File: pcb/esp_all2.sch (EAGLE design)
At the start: 22 parts

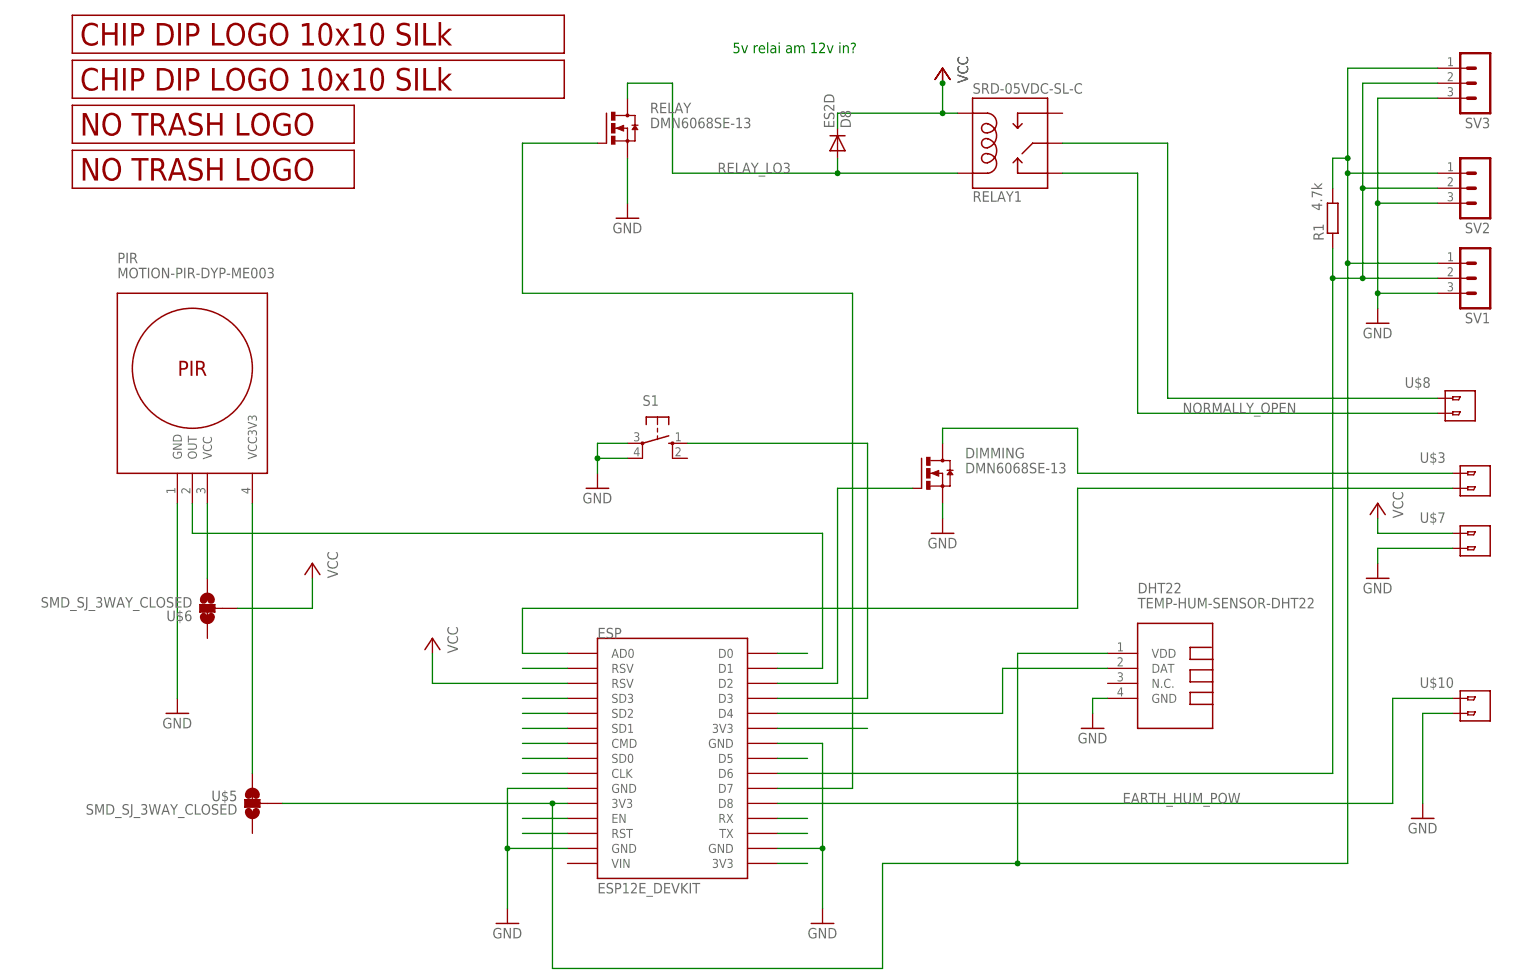
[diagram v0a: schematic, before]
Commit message: Improved ESP readability
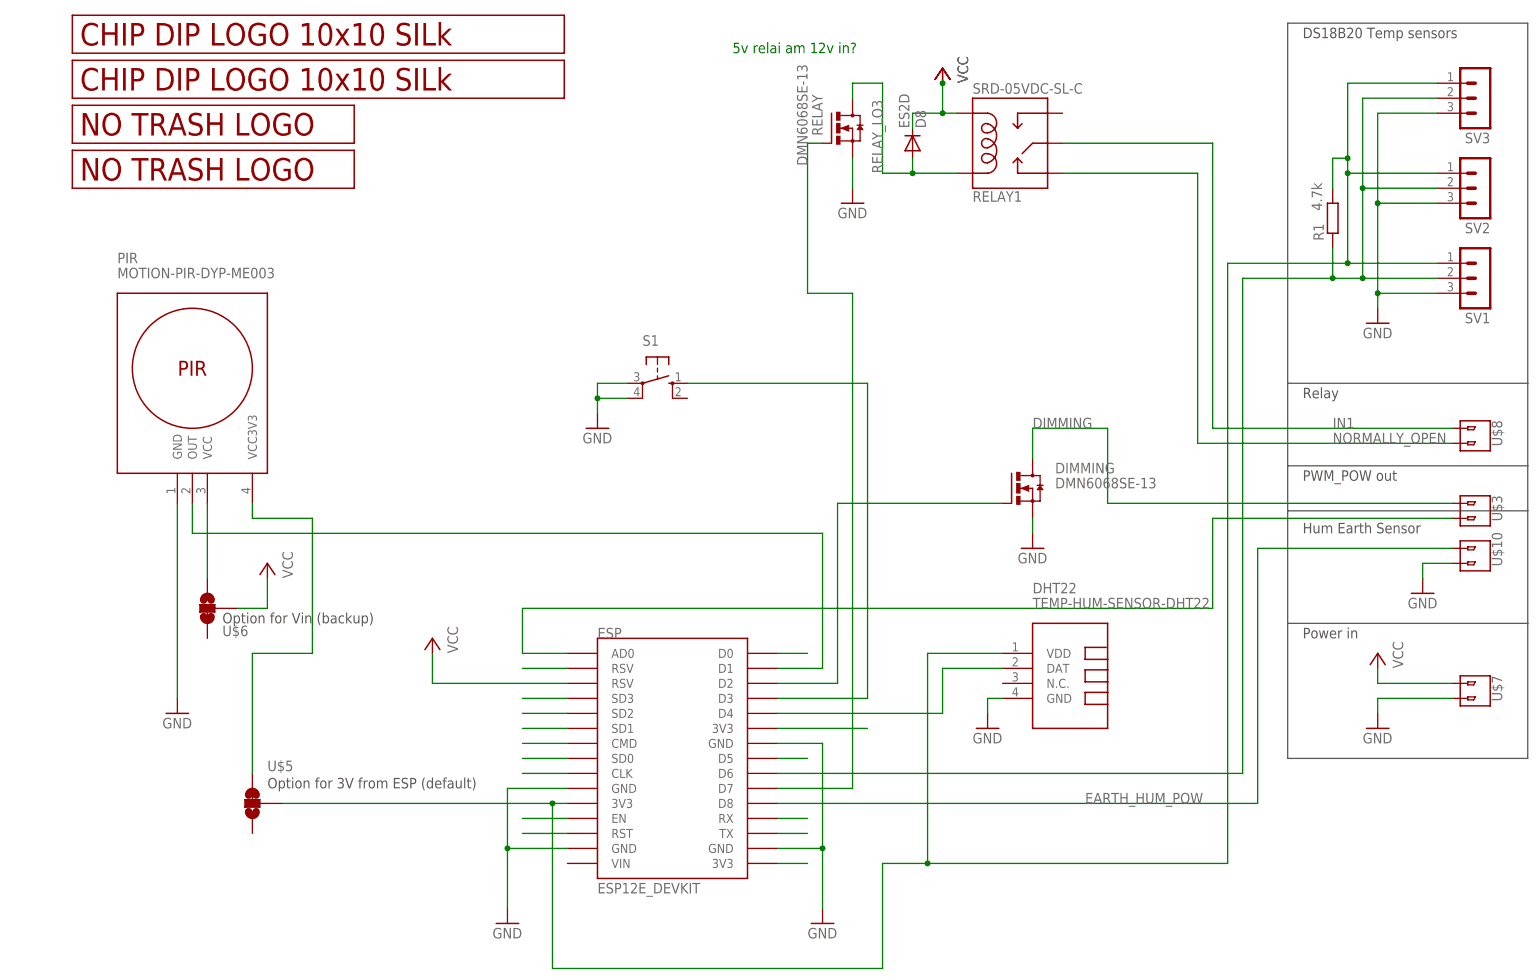
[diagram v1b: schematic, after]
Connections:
- net N$17 renamed DIMMING
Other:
- note added: "DS18B20 Temp sensors"
- note added: "Hum Earth Sensor"
- note added: "Option for 3V from ESP (default)"
- note added: "Option for Vin (backup)"
- note added: "PWM_POW out"
- note added: "Power in"
- note added: "Relay"
- moved on the sheet: D8, DHT22, DIMMING, RELAY, S1, SV3, U$10, U$3, U$7, U$8
